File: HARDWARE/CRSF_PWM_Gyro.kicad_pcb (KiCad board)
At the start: 2 copper layers, 37 parts, among them J1 USB_C_Receptacle_USB2.0_16P, J2 Conn_01x18, U1 TCR2EF33_LMCT, U2 STM32G431KBTx, Y1 Crystal_GND24

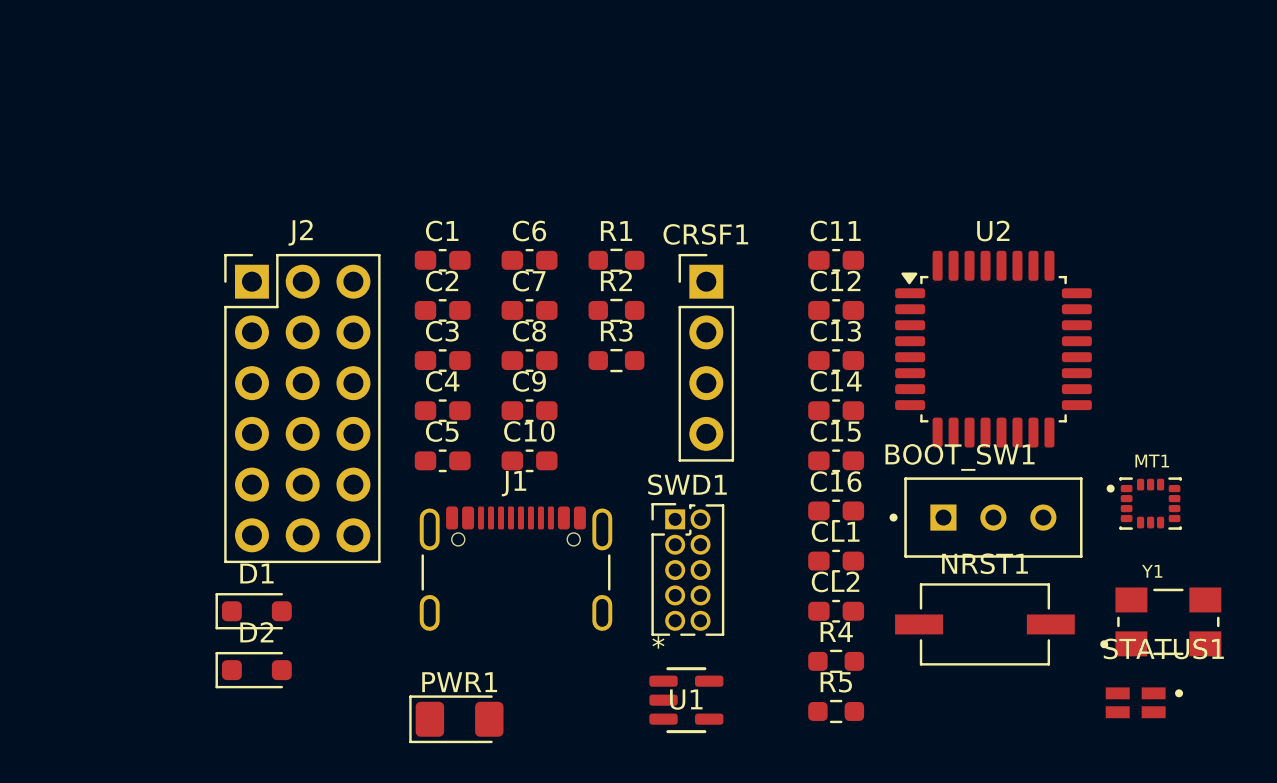
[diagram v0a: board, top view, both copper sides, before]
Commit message: Swap PWM channels and initial PCB layout
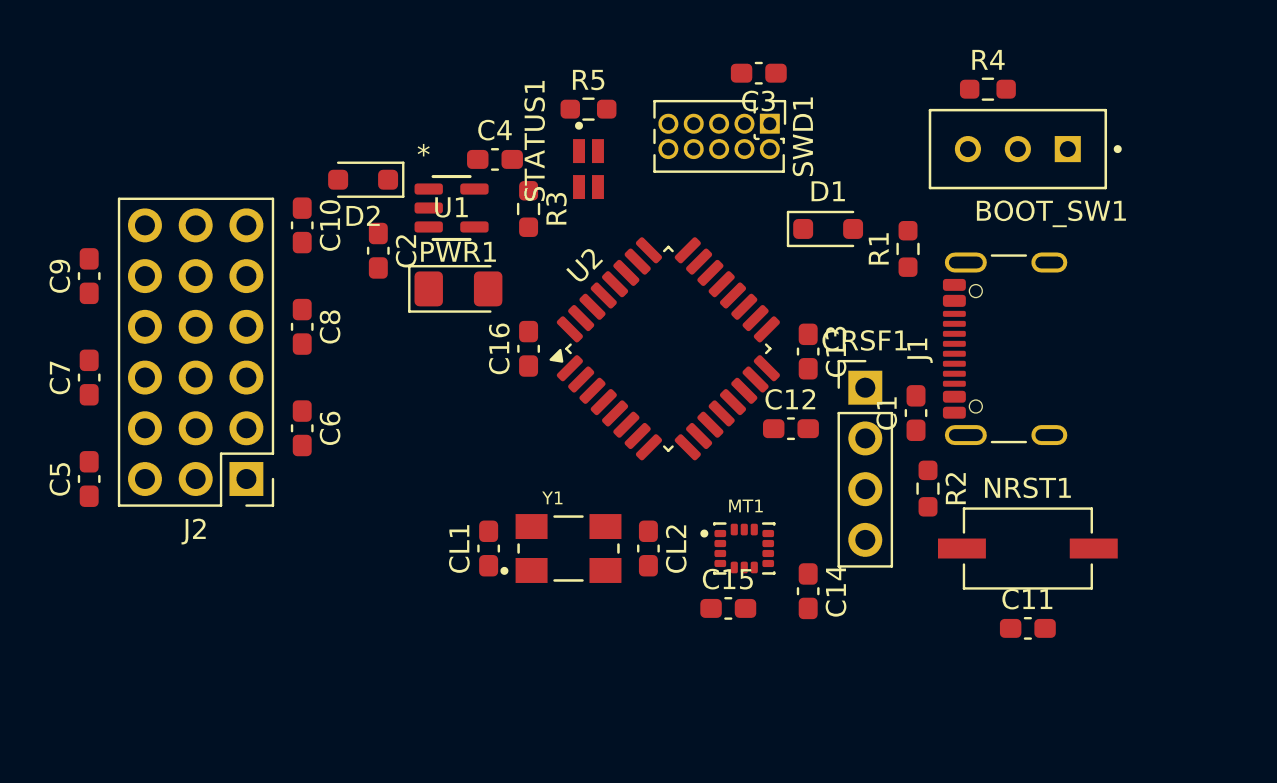
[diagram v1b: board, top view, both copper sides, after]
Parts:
- moved STATUS1 38.3 mm to (136.0, 81.0), turned to 90 degrees
- moved D1 34.4 mm to (148.0, 84.0)
- moved R5 32.6 mm to (136.0, 78.0)
- moved Y1 30.3 mm to (135.0, 100.0)
- moved R4 29.6 mm to (156.0, 77.0)
- moved J1 28.4 mm to (158.0, 90.0), turned to 90 degrees
- moved U1 27.3 mm to (129.1, 83.0)
- moved D2 25.1 mm to (124.7, 81.5), turned to 180 degrees
- moved C1 24.9 mm to (152.4, 93.2), turned to 90 degrees
- moved C9 23.1 mm to (111.0, 86.4), turned to 90 degrees
- moved C7 22.3 mm to (111.0, 91.4), turned to 90 degrees
- moved PWR1 21.6 mm to (129.5, 87.0)
- moved C3 21.4 mm to (144.5, 76.2), turned to 180 degrees
- moved C11 20.8 mm to (158.0, 104.0)
- moved MT1 20.5 mm to (143.8, 100.0)
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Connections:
- J2 pad 1: CH1_PWM -> CH6_PWM
- J2 pad 10: CH4_PWM -> CH3_PWM
- J2 pad 13: CH5_PWM -> CH2_PWM
- J2 pad 16: CH6_PWM -> CH1_PWM
- J2 pad 4: CH2_PWM -> CH5_PWM
- J2 pad 7: CH3_PWM -> CH4_PWM

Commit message: Update components and layout
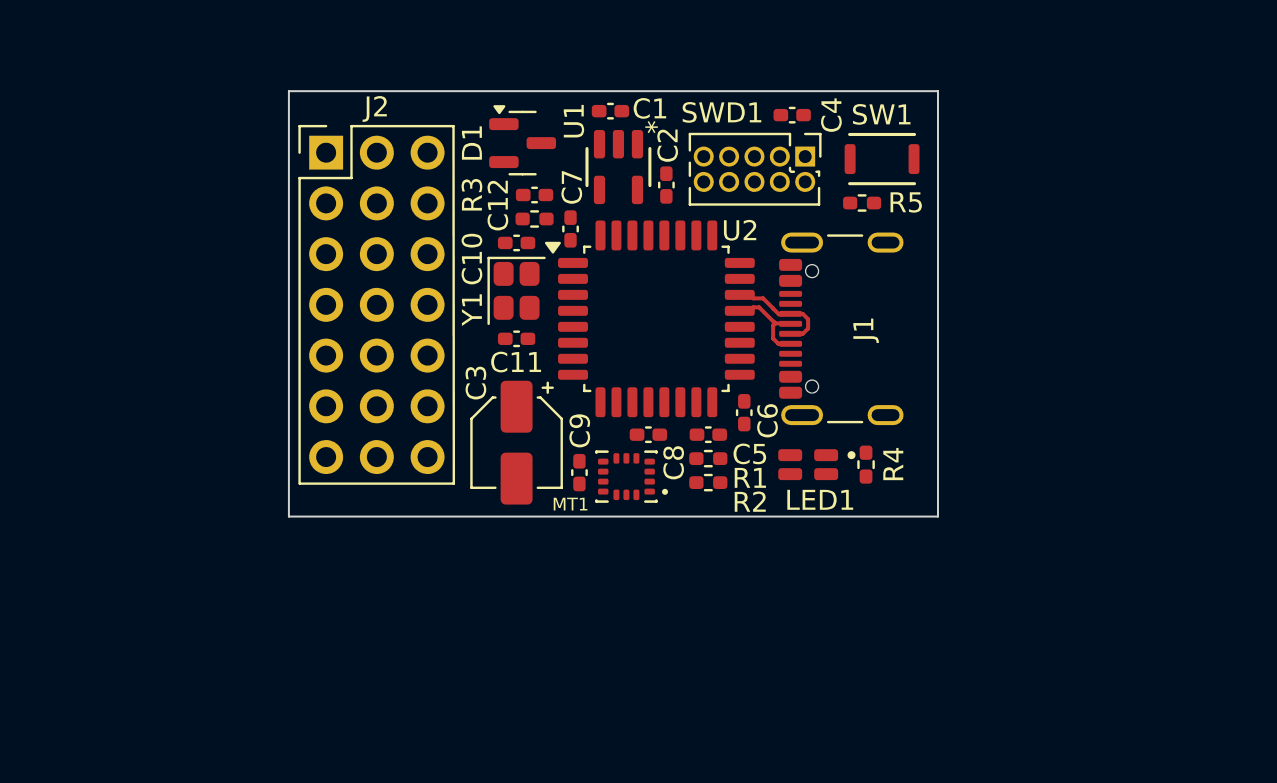
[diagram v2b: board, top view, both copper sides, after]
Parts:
- removed BOOT_SW1: SW_SPDT, Button_Switch_THT_Custom:SW_SLW-883935-2A-D
- removed the C1 at (152.4, 93.2)
- removed the C10 at (121.7, 83.8)
- removed the C11 at (158.0, 104.0)
- removed the C5 at (111.0, 96.5)
- removed the C6 at (121.7, 94.0)
- removed the C7 at (111.0, 91.4)
- removed the C8 at (121.7, 88.9)
- removed the C9 at (111.0, 86.4)
- removed CRSF1: Conn_01x04, Connector_PinHeader_2.54mm:PinHeader_1x04_P2.54mm_Vertical
- removed D2: D_Schottky, Diode_SMD:D_SOD-323_HandSoldering
- removed NRST1: SW_SPST, Button_Switch_SMD_Custom:SW_Tactile_SPST_PTS636SK25FSMTRLFS
- removed PWR1: LED, LED_SMD:LED_1206_3216Metric_Pad1.42x1.75mm_HandSolder
- added C12: 0.1u, Capacitor_SMD:C_0402_1005Metric_Pad0.74x0.62mm_HandSolder, F.Cu at (133.3, 82.3)
- added C3: 22u, Capacitor_SMD:CP_Elec_4x5.4, F.Cu at (132.4, 94.7)
- added SW1: SW_SPST, Button_Switch_SMD_Custom:R-667995_MIT, F.Cu at (150.7, 80.5)
- C1: renamed from C2; footprint Capacitor_SMD:C_0603_1608Metric_Pad1.08x0.95mm_HandSolder -> Capacitor_SMD:C_0402_1005Metric_Pad0.74x0.62mm_HandSolder
- C10: renamed from CL1; footprint Capacitor_SMD:C_0603_1608Metric_Pad1.08x0.95mm_HandSolder -> Capacitor_SMD:C_0402_1005Metric_Pad0.74x0.62mm_HandSolder
- C11: renamed from CL2; footprint Capacitor_SMD:C_0603_1608Metric_Pad1.08x0.95mm_HandSolder -> Capacitor_SMD:C_0402_1005Metric_Pad0.74x0.62mm_HandSolder
- C2: renamed from C4; footprint Capacitor_SMD:C_0603_1608Metric_Pad1.08x0.95mm_HandSolder -> Capacitor_SMD:C_0402_1005Metric_Pad0.74x0.62mm_HandSolder
- C4: renamed from C3; footprint Capacitor_SMD:C_0603_1608Metric_Pad1.08x0.95mm_HandSolder -> Capacitor_SMD:C_0402_1005Metric_Pad0.74x0.62mm_HandSolder
- C5: renamed from C12; footprint Capacitor_SMD:C_0603_1608Metric_Pad1.08x0.95mm_HandSolder -> Capacitor_SMD:C_0402_1005Metric_Pad0.74x0.62mm_HandSolder
- C6: renamed from C13; footprint Capacitor_SMD:C_0603_1608Metric_Pad1.08x0.95mm_HandSolder -> Capacitor_SMD:C_0402_1005Metric_Pad0.74x0.62mm_HandSolder
- C7: renamed from C14; footprint Capacitor_SMD:C_0603_1608Metric_Pad1.08x0.95mm_HandSolder -> Capacitor_SMD:C_0402_1005Metric_Pad0.74x0.62mm_HandSolder
- C8: renamed from C15; footprint Capacitor_SMD:C_0603_1608Metric_Pad1.08x0.95mm_HandSolder -> Capacitor_SMD:C_0402_1005Metric_Pad0.74x0.62mm_HandSolder
- C9: renamed from C16; footprint Capacitor_SMD:C_0603_1608Metric_Pad1.08x0.95mm_HandSolder -> Capacitor_SMD:C_0402_1005Metric_Pad0.74x0.62mm_HandSolder
- D1: value D_Schottky -> PMEG2005CT,215; footprint Diode_SMD:D_SOD-323_HandSoldering -> Package_TO_SOT_SMD:SOT-23
- J2: value Conn_01x18 -> Conn_01x21; footprint Connector_PinHeader_2.54mm_Custom:PinHeader_3x06_P2.54mm_Vertical -> Connector_PinHeader_2.54mm_Custom:PinHeader_3x07_P2.54mm_Vertical
- R1: renamed from R2; footprint Resistor_SMD:R_0603_1608Metric_Pad0.98x0.95mm_HandSolder -> Resistor_SMD:R_0402_1005Metric_Pad0.72x0.64mm_HandSolder
- R2: renamed from R1; footprint Resistor_SMD:R_0603_1608Metric_Pad0.98x0.95mm_HandSolder -> Resistor_SMD:R_0402_1005Metric_Pad0.72x0.64mm_HandSolder
- R3: value 1k -> 10k; footprint Resistor_SMD:R_0603_1608Metric_Pad0.98x0.95mm_HandSolder -> Resistor_SMD:R_0402_1005Metric_Pad0.72x0.64mm_HandSolder
- R4: renamed from R5; footprint Resistor_SMD:R_0603_1608Metric_Pad0.98x0.95mm_HandSolder -> Resistor_SMD:R_0402_1005Metric_Pad0.72x0.64mm_HandSolder
- R5: renamed from R4; footprint Resistor_SMD:R_0603_1608Metric_Pad0.98x0.95mm_HandSolder -> Resistor_SMD:R_0402_1005Metric_Pad0.72x0.64mm_HandSolder
- Y1: footprint Crystal_Custom:XTAL_ECS-80-10-30B-CKM-TR -> Crystal_Custom:Crystal_SMD_ECS_ECX_2236-4Pin_2.5x2.0mm
- moved R4 22.6 mm to (149.9, 95.8), turned to -90 degrees
- moved C7 21.7 mm to (135.1, 84.0), turned to 90 degrees
- moved LED1 18.4 mm to (147.0, 95.8), turned to 0 degrees
- moved J2 16.8 mm to (122.9, 80.2), turned to 0 degrees
- moved D1 15.9 mm to (132.7, 79.7)
- moved R2 15.4 mm to (142.0, 96.7), turned to 180 degrees
- moved C10 15.4 mm to (132.4, 84.7), turned to 0 degrees
- moved C1 13.6 mm to (137.1, 78.1), turned to 0 degrees
- moved Y1 13.2 mm to (132.4, 87.1), turned to -90 degrees
- moved C11 12.4 mm to (132.4, 89.5), turned to 180 degrees
- moved R1 11.1 mm to (142.0, 95.5), turned to 180 degrees
- moved C8 9.58 mm to (139.0, 94.3)
- moved C2 8.68 mm to (139.9, 81.8), turned to 90 degrees
- moved U1 8.60 mm to (137.5, 80.9), turned to -90 degrees
- moved R5 8.50 mm to (149.7, 82.7)
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- renumbered STATUS1 to LED1
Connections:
- D1 pad 1: Net-(D1-K) -> V_ESC
- J2 pad 1: CH6_PWM -> GND
- J2 pad 10: CH3_PWM -> GND
- J2 pad 12: GND -> CH3_PWM
- J2 pad 13: CH2_PWM -> GND
- J2 pad 15: GND -> CH2_PWM
- J2 pad 16: CH1_PWM -> GND
- J2 pad 18: GND -> CH1_PWM
- J2 pad 3: GND -> CH6_PWM
- J2 pad 4: CH5_PWM -> GND
- J2 pad 6: GND -> CH5_PWM
- J2 pad 7: CH4_PWM -> GND
- J2 pad 9: GND -> CH4_PWM
- R3 pad 2: Net-(PWR1-A) -> N_RESET
- R5 pad 2: Net-(BOOT_SW1-B) -> GND
- U2 pad 19: CRSF_MCU_to_RX -> unconnected-(U2-PA9-Pad19)
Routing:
- net USB_D+: track 0.00 -> 5.40 mm
- net USB_D-: track 0.00 -> 4.75 mm
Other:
- board outline added: 32.5 x 21.3 mm

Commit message: Made footprint updates
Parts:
- moved C8 1.20 mm to (137.8, 94.3), turned to 180 degrees
- moved MT1 0.06 mm to (137.9, 96.3)
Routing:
- net USB_D+: track 5.40 -> 0.00 mm
- net USB_D-: track 4.75 -> 0.00 mm

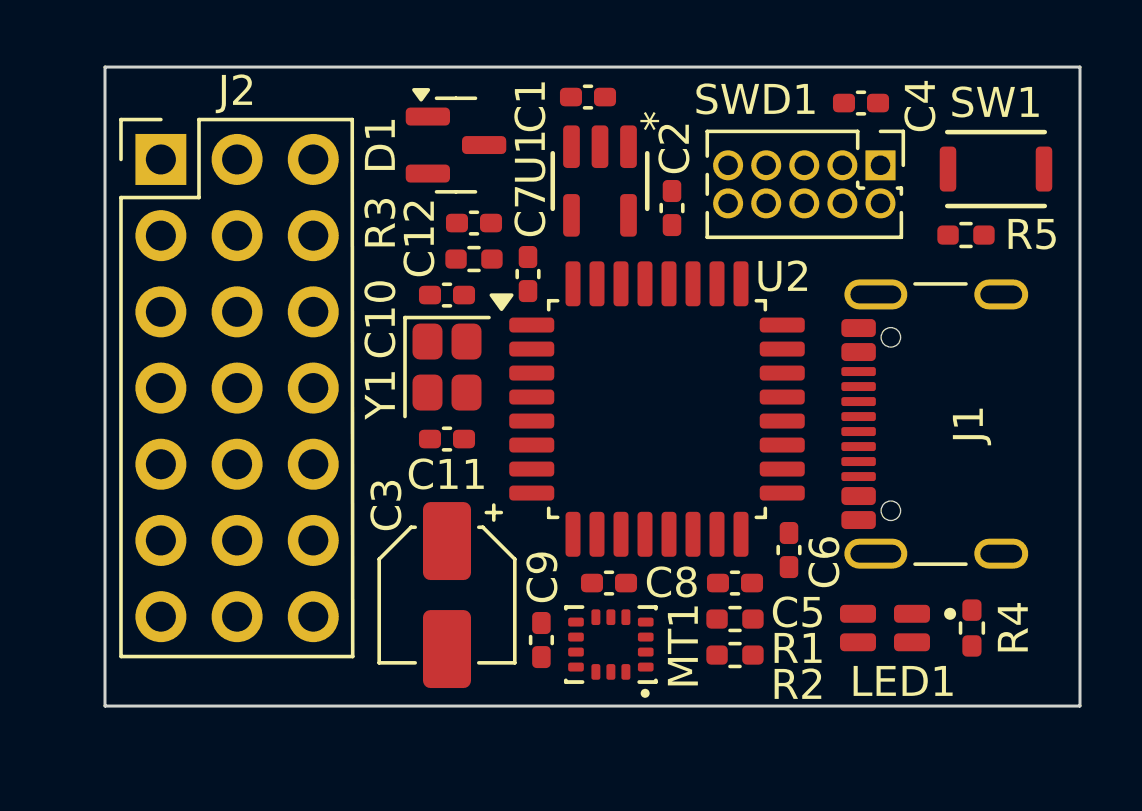
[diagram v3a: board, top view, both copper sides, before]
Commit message: Complete initial routing
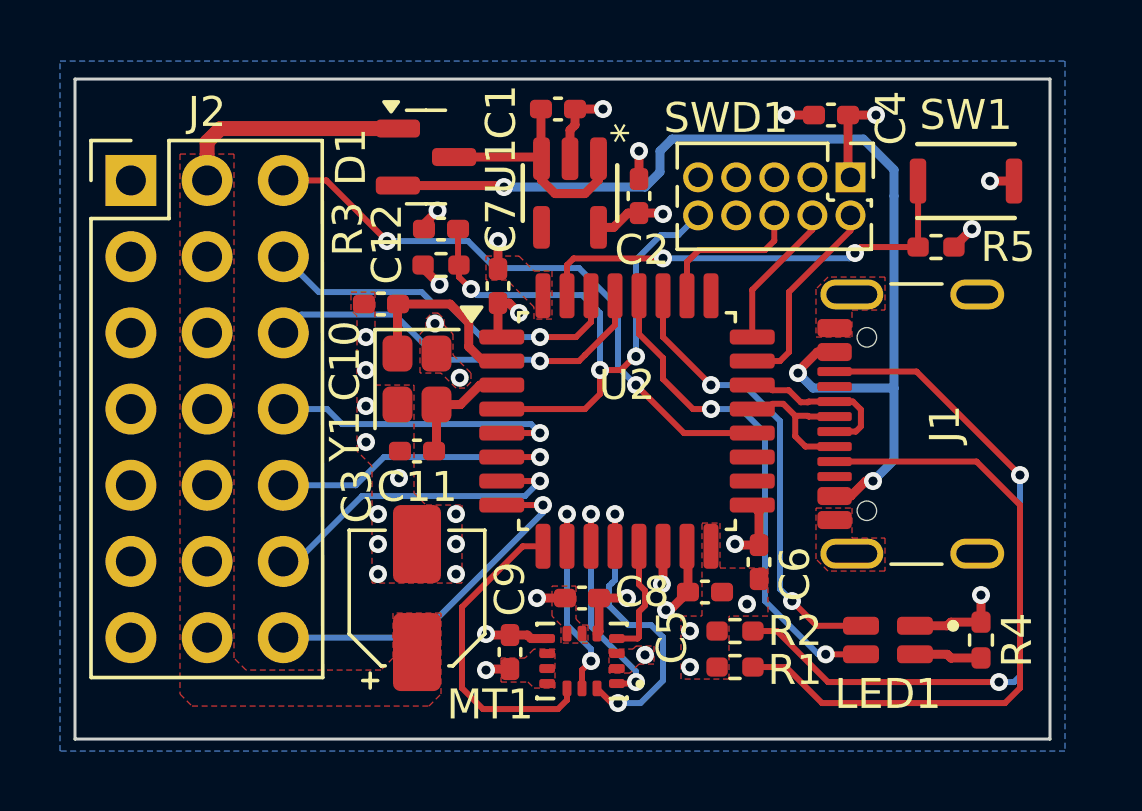
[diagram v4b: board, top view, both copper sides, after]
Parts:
- moved C10 2.22 mm to (130.2, 85.0), turned to 180 degrees
- moved R1 1.60 mm to (142.0, 97.1)
- moved J2 1.22 mm to (121.9, 80.9)
- moved C2 1.17 mm to (138.8, 81.4)
- moved C9 1.12 mm to (134.5, 96.6)
- moved C12 1.12 mm to (132.2, 82.5)
- moved R3 1.12 mm to (132.2, 83.7)
- moved MT1 1.11 mm to (136.9, 96.9)
- moved C1 1.08 mm to (136.1, 78.5)
- moved C11 1.08 mm to (131.4, 89.9)
- moved C4 1.08 mm to (145.2, 78.7)
- moved C7 1.08 mm to (134.1, 84.4)
- moved SW1 1.08 mm to (149.7, 80.9)
- moved SWD1 1.08 mm to (145.8, 80.8)
- moved U2 1.08 mm to (138.4, 88.9)
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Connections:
- J2 pad 15: CH2_PWM -> CH4_PWM
- J2 pad 18: CH1_PWM -> CH5_PWM
- J2 pad 21: CRSF_RX_To_MCU -> CH6_PWM
- J2 pad 3: CH6_PWM -> CRSF_RX_To_MCU
- J2 pad 6: CH5_PWM -> CH1_PWM
- J2 pad 9: CH4_PWM -> CH2_PWM
- U2 pad 27: STATUS_LED_RED -> STATUS_LED_BLUE
- U2 pad 28: STATUS_LED_BLUE -> STATUS_LED_RED
- U2 pad 29: CH1_PWM -> CH2_PWM
- U2 pad 30: CH2_PWM -> CH1_PWM
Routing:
- net Net-(D1-A-Pad2): track 0.00 -> 35.2 mm, vias 0 -> 3
- net Net-(J1-CC2): track 0.00 -> 24.0 mm, vias 0 -> 2
- net Net-(J1-CC1): track 0.00 -> 22.5 mm
- net +3.3V: track 0.00 -> 21.3 mm, vias 0 -> 10
- net CRSF_RX_To_MCU: track 0.00 -> 20.3 mm, vias 0 -> 2
- net N_RESET: track 0.00 -> 20.3 mm, vias 0 -> 3
- net STATUS_LED_RED: track 0.00 -> 16.8 mm, vias 0 -> 2
- net STATUS_LED_BLUE: track 0.00 -> 15.2 mm, vias 0 -> 2
- net Net-(SW1-A): track 0.00 -> 15.2 mm, vias 0 -> 2
- net CH2_PWM: track 0.00 -> 13.4 mm, vias 0 -> 1
- net CH1_PWM: track 0.00 -> 12.4 mm, vias 0 -> 1
- net CH6_PWM: track 0.00 -> 12.0 mm, vias 0 -> 1
- net CH5_PWM: track 0.00 -> 10.9 mm, vias 0 -> 1
- net Net-(MT1-AP_SDA/AP_SDIO/AP_SDI): track 0.00 -> 10.6 mm, vias 0 -> 2
- net Net-(MT1-AP_CS): track 0.00 -> 10.5 mm
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- added copper zone on B.Cu, net +3.3V
- added copper zone on F.Cu, net GND
- added copper zone on In1.Cu, net GND
- added copper zone on In2.Cu, net GND
- added copper zone on F.Cu, net V_ESC
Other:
- board size 32.5 x 21.3 mm -> 32.5 x 22 mm
- copper layers 2 -> 4

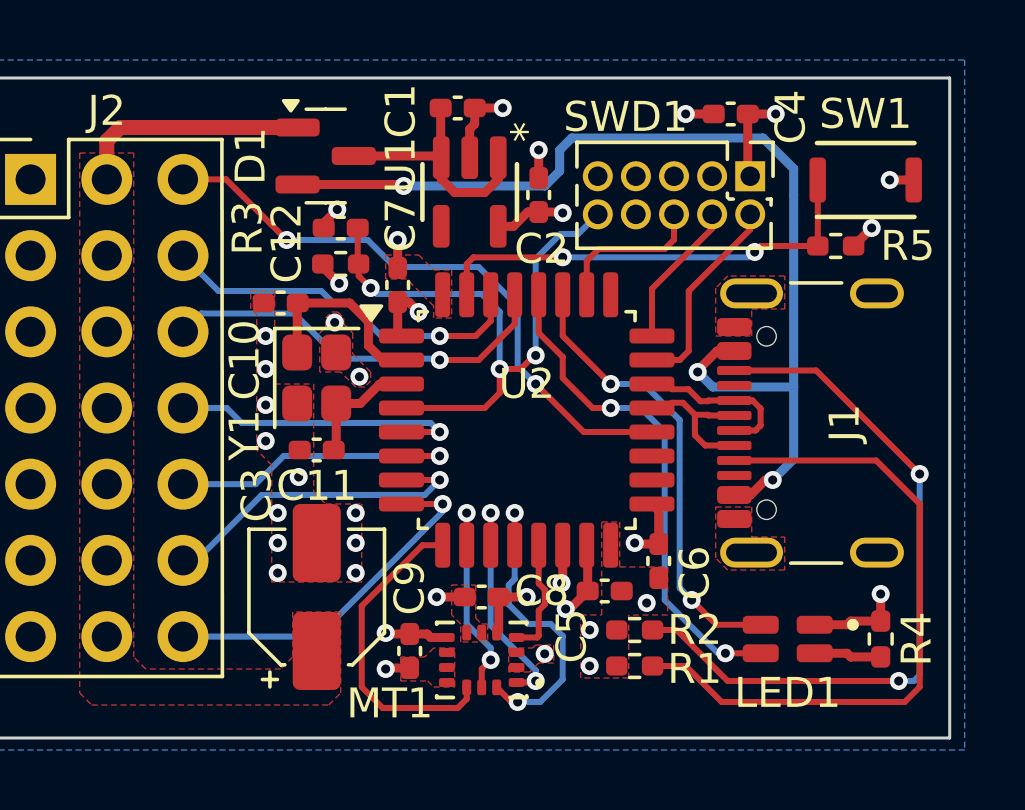
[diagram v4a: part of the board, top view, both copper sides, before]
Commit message: Make minor routing changes
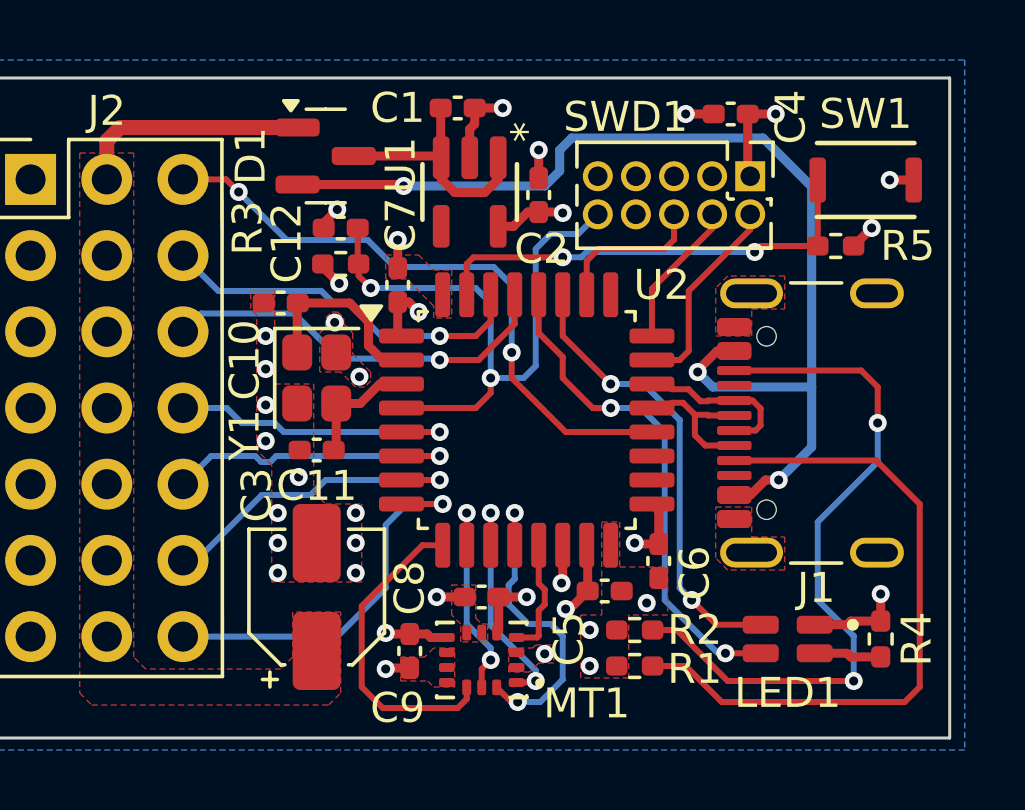
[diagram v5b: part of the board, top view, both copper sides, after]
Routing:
- net Net-(D1-A-Pad2): track 35.2 -> 36.4 mm
- net CH6_PWM: track 12.0 -> 13.1 mm
- net CRSF_RX_To_MCU: track 20.3 -> 20.9 mm
- net N_RESET: track 20.3 -> 20.7 mm, vias 3 -> 2

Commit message: Add other fields to BOM
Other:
- board text added: "CH1"
- board text added: "CH2"
- board text added: "CH3"
- board text added: "CH4"
- board text added: "CH5"
- board text added: "CH6"
- board text added: "Gyro v1.0"
- board text added: "SER"
